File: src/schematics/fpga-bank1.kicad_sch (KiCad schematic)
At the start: 1 part

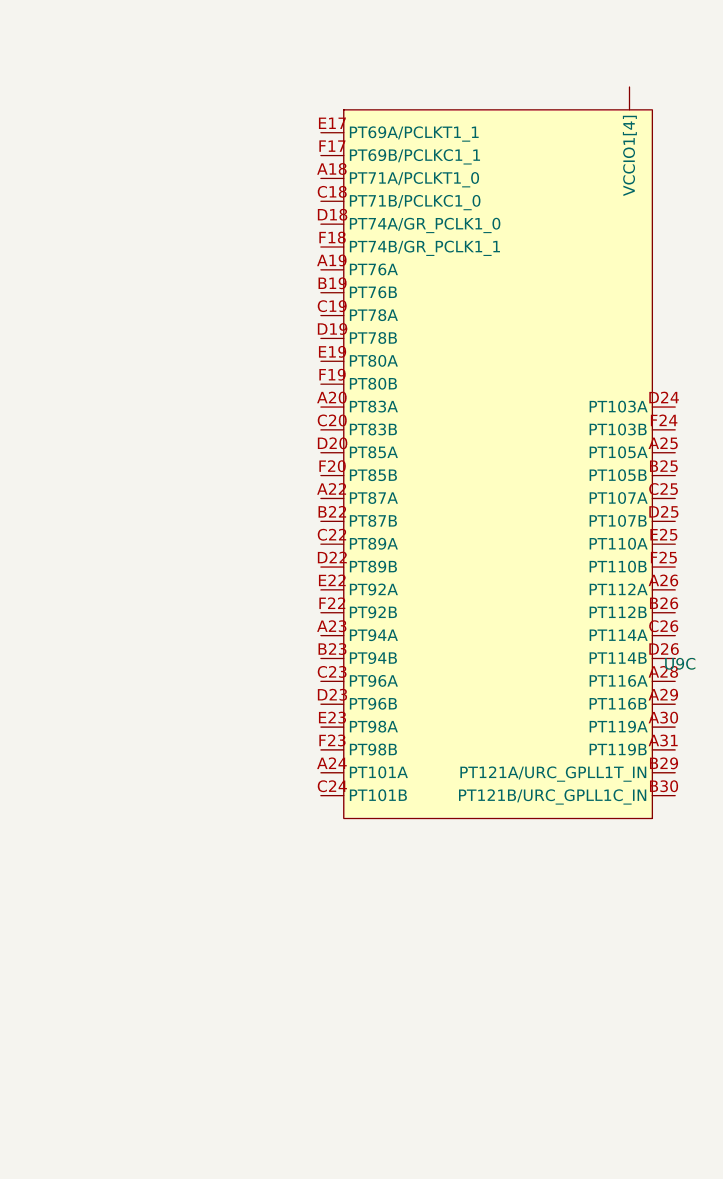
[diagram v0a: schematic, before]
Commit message: Draft connections between the FPGA and the memories
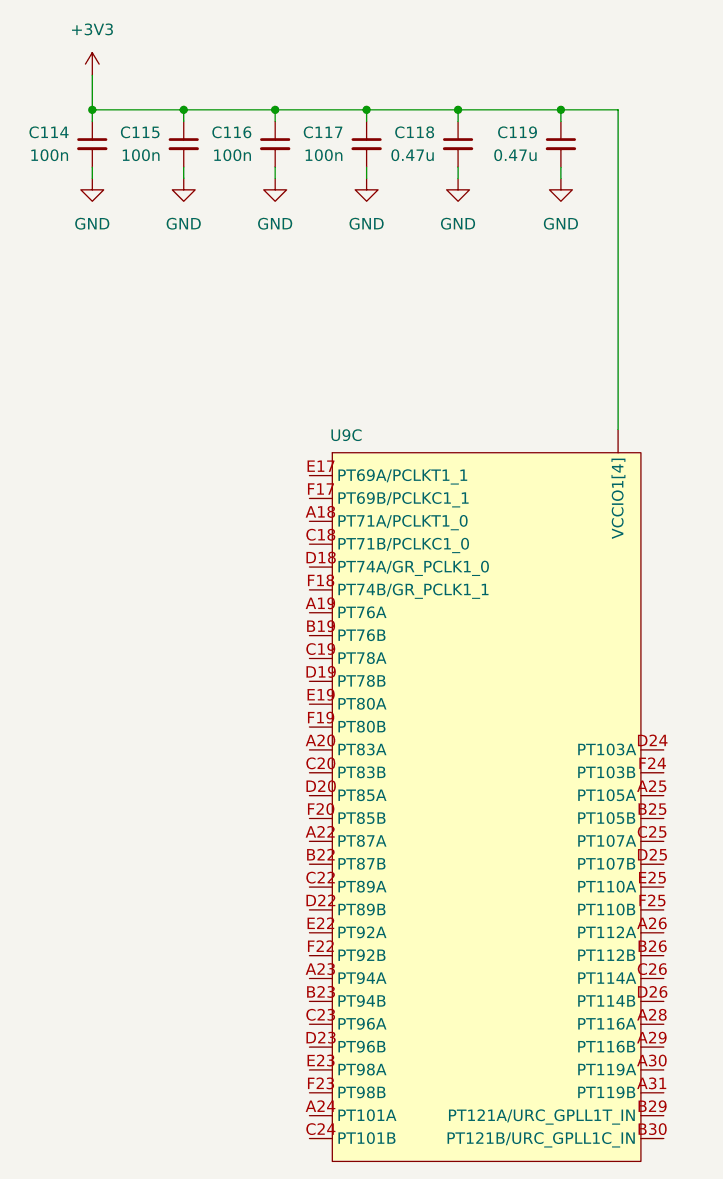
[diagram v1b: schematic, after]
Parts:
- added C114, C115, C116, C117: 100n, symbol Device:C_Small
- added C118, C119: 0.47u, symbol Device:C_Small
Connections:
- net VCCIO1 renamed +3V3
- net +3V3: now also C114.1, C115.1, C116.1, C117.1, C118.1, C119.1
- new net GND: C114.2, C115.2, C116.2, C117.2, C118.2, C119.2
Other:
- moved on the sheet: U9C

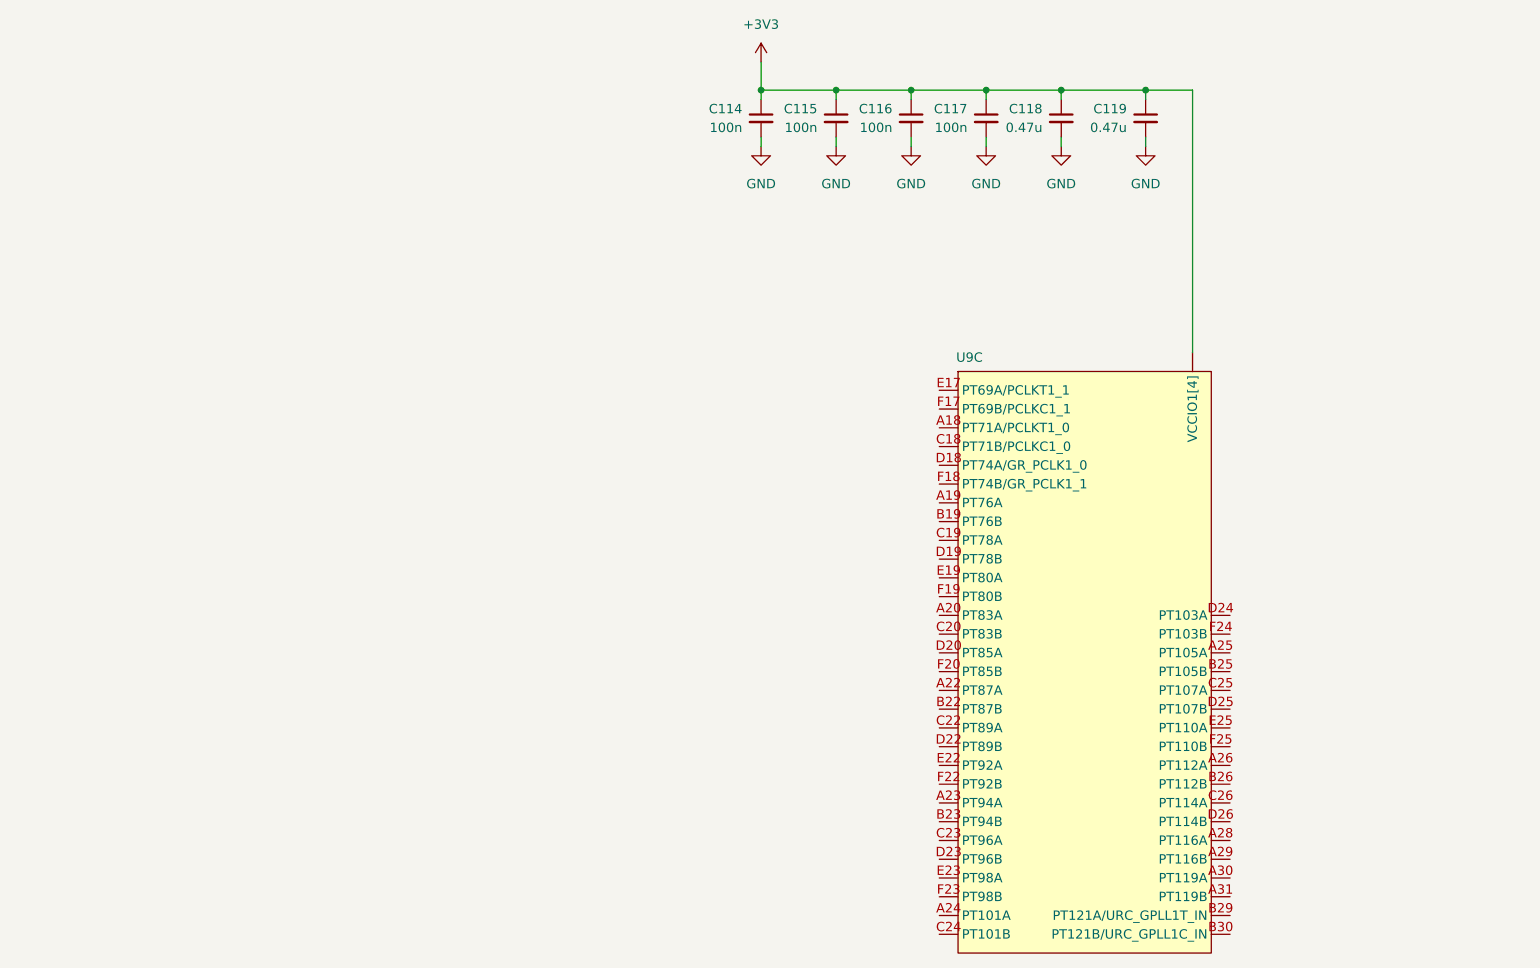
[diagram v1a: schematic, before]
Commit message: Adds draft of IO connector schematic connections to FPGA
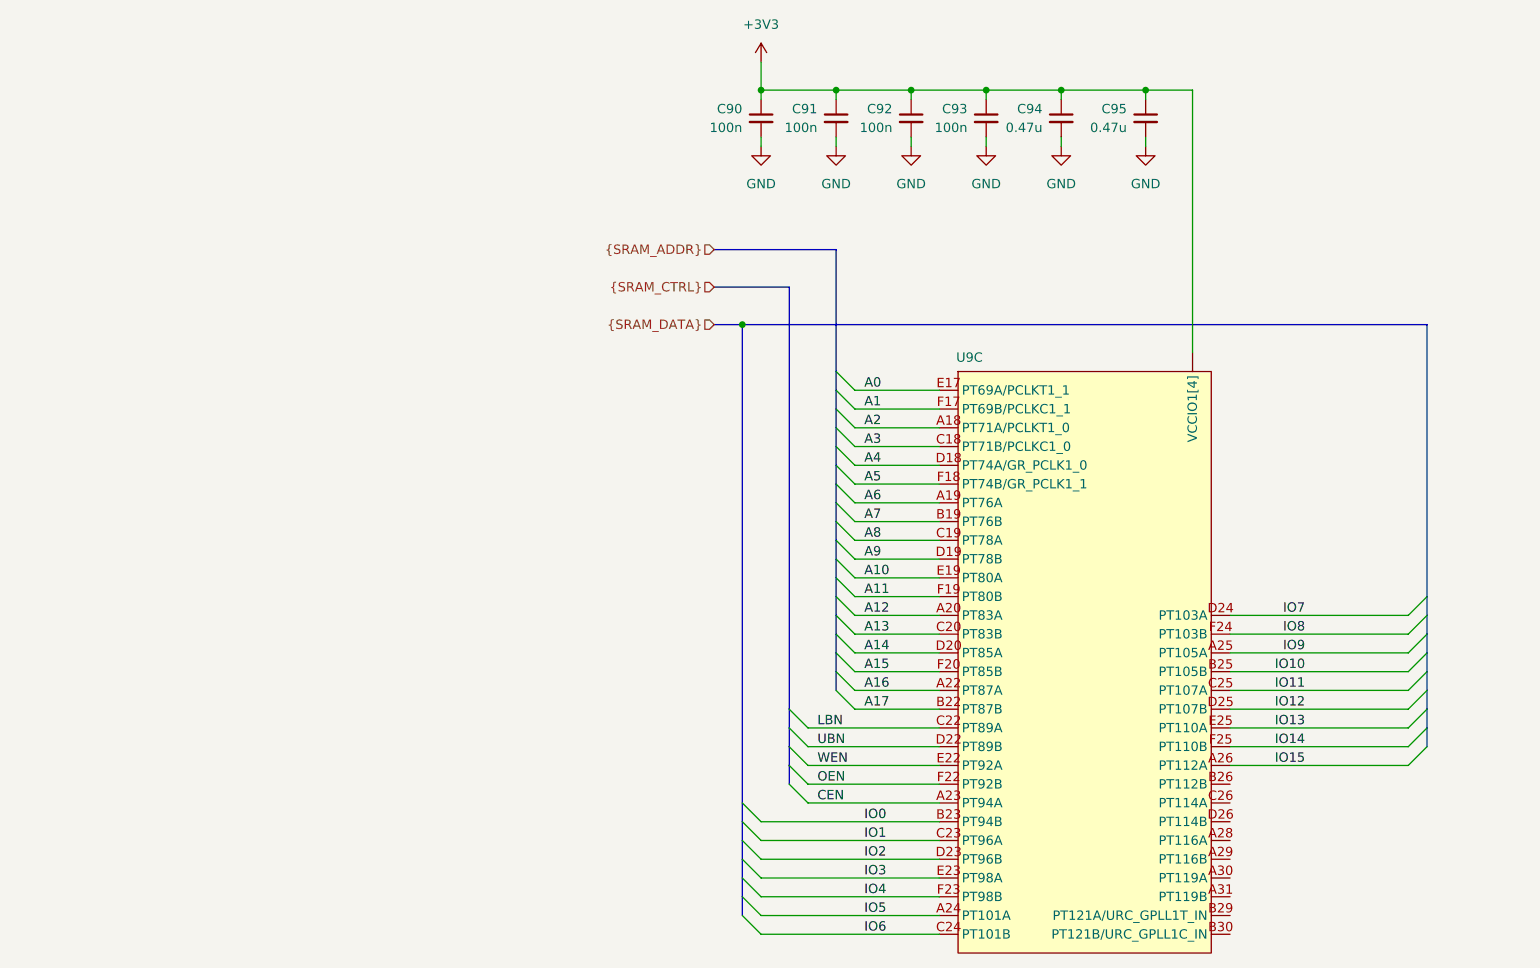
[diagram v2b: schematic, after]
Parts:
- removed C114, C115, C116, C117: 100n, symbol Device:C_Small
- removed C118, C119: 0.47u, symbol Device:C_Small
- added C90, C91, C92, C93: 100n, symbol Device:C_Small
- added C94, C95: 0.47u, symbol Device:C_Small
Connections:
- net +3V3: now also C90.1, C91.1, C92.1, C93.1, C94.1, C95.1
- net GND: now also C90.2, C91.2, C92.2, C93.2, C94.2, C95.2
- net A2: now reaches U9.A18 (PT71A/PCLKT1_0)
- net A6: now reaches U9.A19 (PT76A)
- net A12: now reaches U9.A20 (PT83A)
- net A16: now reaches U9.A22 (PT87A)
- net CEN: now reaches U9.A23 (PT94A)
- net IO5: now reaches U9.A24 (PT101A)
- net IO9: now reaches U9.A25 (PT105A)
- net IO15: now reaches U9.A26 (PT112A)
- net A7: now reaches U9.B19 (PT76B)
- net A17: now reaches U9.B22 (PT87B)
- net IO0: now reaches U9.B23 (PT94B)
- net IO10: now reaches U9.B25 (PT105B)
- net A3: now reaches U9.C18 (PT71B/PCLKC1_0)
- net A8: now reaches U9.C19 (PT78A)
- net A13: now reaches U9.C20 (PT83B)
- net LBN: now reaches U9.C22 (PT89A)
- net IO1: now reaches U9.C23 (PT96A)
- net IO6: now reaches U9.C24 (PT101B)
- net IO11: now reaches U9.C25 (PT107A)
- net A4: now reaches U9.D18 (PT74A/GR_PCLK1_0)
- net A9: now reaches U9.D19 (PT78B)
- net A14: now reaches U9.D20 (PT85A)
- net UBN: now reaches U9.D22 (PT89B)
- net IO2: now reaches U9.D23 (PT96B)
- net IO7: now reaches U9.D24 (PT103A)
- net IO12: now reaches U9.D25 (PT107B)
- net A0: now reaches U9.E17 (PT69A/PCLKT1_1)
- net A10: now reaches U9.E19 (PT80A)
- net WEN: now reaches U9.E22 (PT92A)
- net IO3: now reaches U9.E23 (PT98A)
- net IO13: now reaches U9.E25 (PT110A)
- net A1: now reaches U9.F17 (PT69B/PCLKC1_1)
- net A5: now reaches U9.F18 (PT74B/GR_PCLK1_1)
- net A11: now reaches U9.F19 (PT80B)
- net A15: now reaches U9.F20 (PT85B)
- net OEN: now reaches U9.F22 (PT92B)
- net IO4: now reaches U9.F23 (PT98B)
- net IO8: now reaches U9.F24 (PT103B)
- net IO14: now reaches U9.F25 (PT110B)

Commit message: Adds the clock oscillator
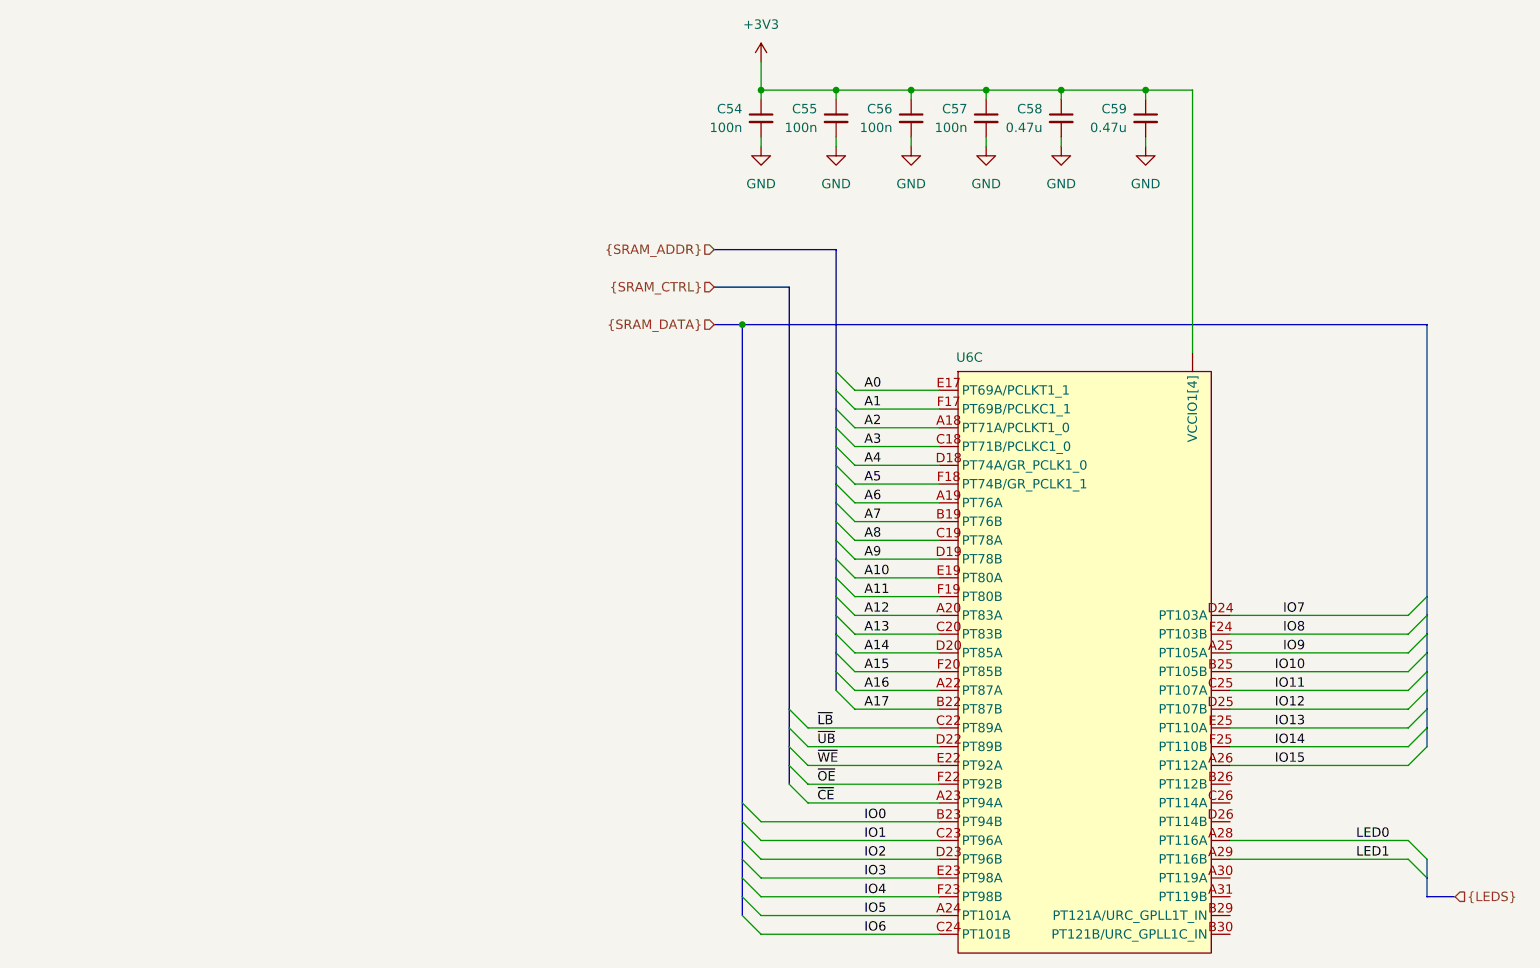
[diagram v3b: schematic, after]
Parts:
- removed U9: ~, symbol ECAP5-BSOM:LFE5U-85F-*BG756*
- added U6: ~, symbol ECAP5-BSOM:LFE5U-85F-*BG756*
- renumbered C90 to C54, C91 to C55, C92 to C56, C93 to C57, C94 to C58, C95 to C59
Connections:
- net +3V3: now also U6. (VCCIO1[4]), U6.K17 (VCCIO1), U6.K18 (VCCIO1), U6.K19 (VCCIO1), U6.K21 (VCCIO1)
- net A0: now also U6.E17 (PT69A/PCLKT1_1)
- net A1: now also U6.F17 (PT69B/PCLKC1_1)
- net A10: now also U6.E19 (PT80A)
- net A11: now also U6.F19 (PT80B)
- net A12: now also U6.A20 (PT83A)
- net A13: now also U6.C20 (PT83B)
- net A14: now also U6.D20 (PT85A)
- net A15: now also U6.F20 (PT85B)
- net A16: now also U6.A22 (PT87A)
- net A17: now also U6.B22 (PT87B)
- net A2: now also U6.A18 (PT71A/PCLKT1_0)
- net A3: now also U6.C18 (PT71B/PCLKC1_0)
- net A4: now also U6.D18 (PT74A/GR_PCLK1_0)
- net A5: now also U6.F18 (PT74B/GR_PCLK1_1)
- net A6: now also U6.A19 (PT76A)
- net A7: now also U6.B19 (PT76B)
- net A8: now also U6.C19 (PT78A)
- net A9: now also U6.D19 (PT78B)
- net IO0: now also U6.B23 (PT94B)
- net IO1: now also U6.C23 (PT96A)
- net IO10: now also U6.B25 (PT105B)
- net IO11: now also U6.C25 (PT107A)
- net IO12: now also U6.D25 (PT107B)
- net IO13: now also U6.E25 (PT110A)
- net IO14: now also U6.F25 (PT110B)
- net IO15: now also U6.A26 (PT112A)
- net IO2: now also U6.D23 (PT96B)
- net IO3: now also U6.E23 (PT98A)
- net IO4: now also U6.F23 (PT98B)
- net IO5: now also U6.A24 (PT101A)
- net IO6: now also U6.C24 (PT101B)
- net IO7: now also U6.D24 (PT103A)
- net IO8: now also U6.F24 (PT103B)
- net IO9: now also U6.A25 (PT105A)
- new net LED0: U6.A28 (PT116A)
- new net LED1: U6.A29 (PT116B)
- new net ~{CE}: U6.A23 (PT94A)
- new net ~{LB}: U6.C22 (PT89A)
- new net ~{OE}: U6.F22 (PT92B)
- new net ~{UB}: U6.D22 (PT89B)
- new net ~{WE}: U6.E22 (PT92A)

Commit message: Adds bus aliases
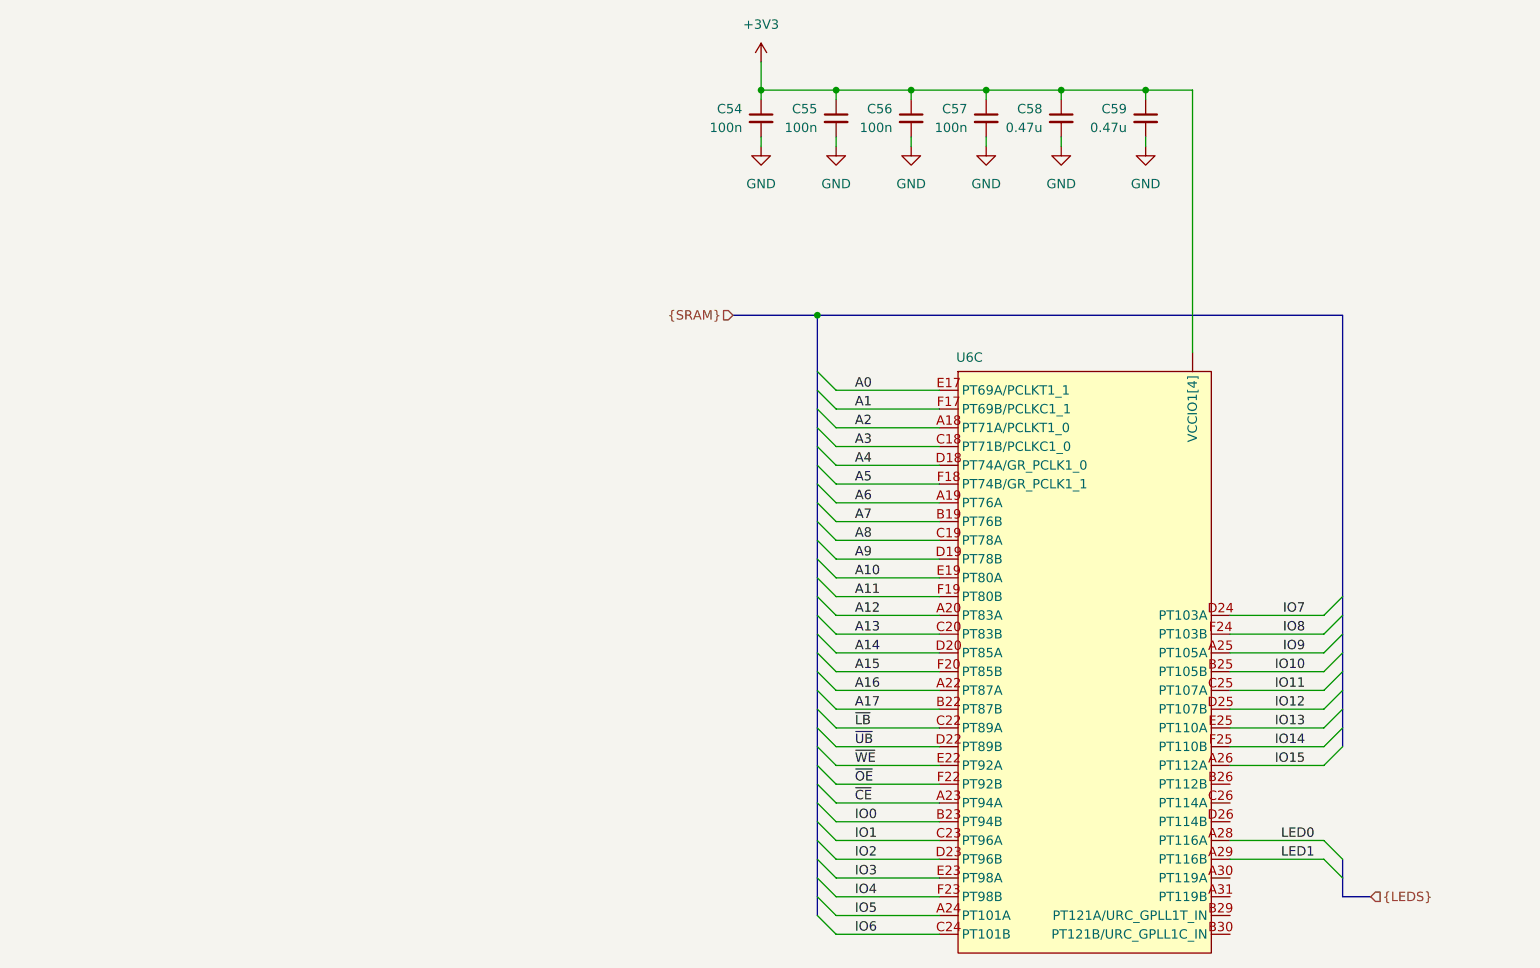
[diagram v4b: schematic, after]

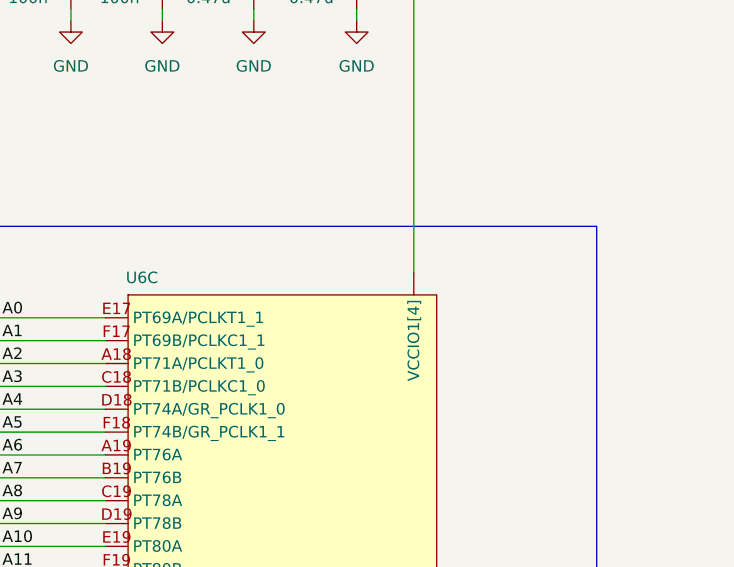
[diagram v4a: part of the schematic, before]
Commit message: Fix some ERC issues
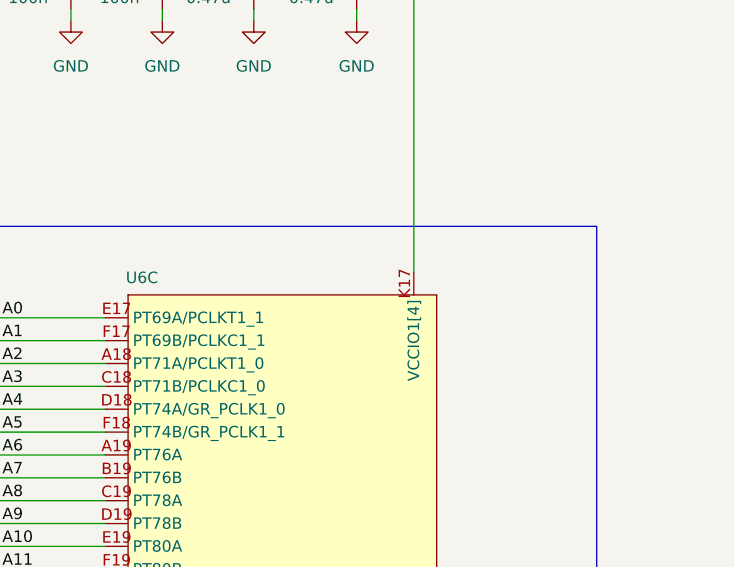
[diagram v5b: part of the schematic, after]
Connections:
- net +3V3: no longer U6. (VCCIO1[4])
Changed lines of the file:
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@@
 		(pin "Y31"
 		)
-		(pin ""
-		)
 		(pin "A10"
 		)
@@
 		(pin "Y32"
 		)
-		(pin ""
-		)
 		(pin "AB23"
 		)
@@
 		(pin "K16"
 		)
-		(pin ""
-		)
 		(pin "A18"
 		)
@@
 		(pin "K21"
 		)
-		(pin ""
-		)
 		(pin "B32"
 		)
@@
 		(pin "T23"
 		)
-		(pin ""
-		)
 		(pin "AA23"
 		)
@@
 		(pin "AM31"
 		)
-		(pin ""
-		)
 		(pin "AA10"
 		)
@@
 		(pin "Y7"
 		)
-		(pin ""
-		)
 		(pin "B1"
 		)
@@
 		(pin "T10"
 		)
-		(pin ""
-		)
 		(pin "AB10"
 		)
@@
 		(pin "M14"
 		)
-		(pin ""
-		)
 		(pin "AH12"
 		)
@@
 		(pin "V19"
 		)
-		(pin ""
-		)
 		(pin "AC11"
 		)
@@
 		(pin "AA11"
 		)
-		(pin ""
-		)
 		(instances
